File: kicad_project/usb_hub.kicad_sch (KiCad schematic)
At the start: 55 parts, among them J1 USB4105-GF-A, J2 UJ2-ADH-3-TH, U2 CY7C65632-48AXCT, U3 USBLC6-2SC6, U4 USBLC6-2SC6, U5 USBLC6-2SC6, U6 BD2221G-LBTR, U7 BD2221G-LBTR, X1 12.000MHz

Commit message: Kate's suggestions, part 1
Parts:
- removed C1, C2: 100nF, Capacitor_SMD:C_1206_3216Metric, symbol Device:C_Small
- removed C5, C8: 1u, Capacitor_SMD:C_1206_3216Metric, symbol Device:C_Small
- removed X1: 12.000MHz, Oscillator:Oscillator_SMD_Abracon_ASV-4Pin_7.0x5.1mm, symbol Oscillator:ASV-xxxMHz
- added C33, C34: 2.2uF, Capacitor_SMD:C_1206_3216Metric, symbol Device:C_Small
- added R48, R49: 1, Resistor_SMD:R_1206_3216Metric, symbol Device:R_US
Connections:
- net GND: now also R48.1, R49.1
- net HUB_VDD_A: now also C33.2, C34.2
- new net: C33.1, R48.2
- new net: C34.1, R49.2
- no-connect marks 9 -> 8
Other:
- note added: "Based on the reference design and review feedback, I assume that needed debouncing is: - 1x 10uF and 1x 1uF on VREG (which I assume is needed only if the internal regulator is used) - A 100nF for each VCC_A pin, plus 2x (2.2uF + 1 Ohm) on VCC_A, plus a ferrite bead - A 100nF for each VCC_D, plus a ferrite bead"
- note removed: "12MHz CMOS Oscillator"
- note removed: "The reference design seems to recommend: - 1x 10uF and 1x 1uF on VREG (which I assume is needed only if the internal regulator is used) - A 100nF for each VCC_A pin, plus 2x 1uF on VCC_A, plus a ferrite bead - A 100nF for each VCC_D, plus a ferrite bead"
- moved on the sheet: C3, C4, C6, C7, FB1, FB2

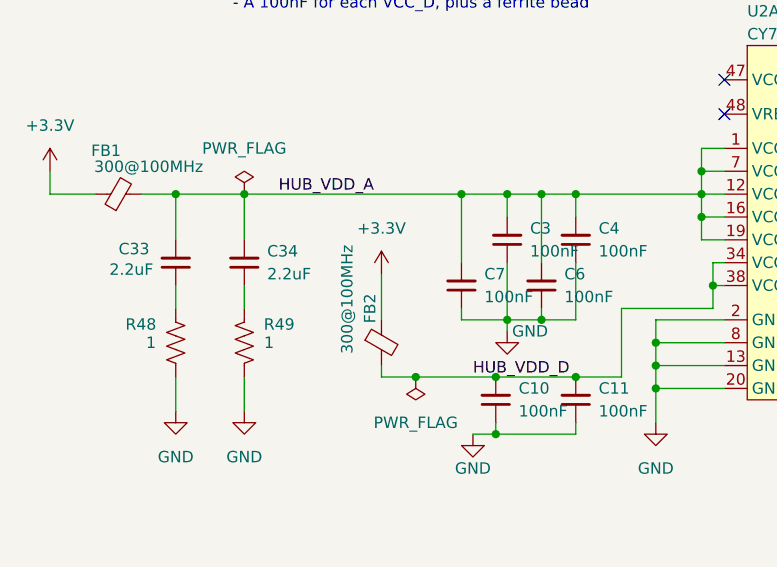
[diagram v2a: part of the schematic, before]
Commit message: Fix some unrouted nets
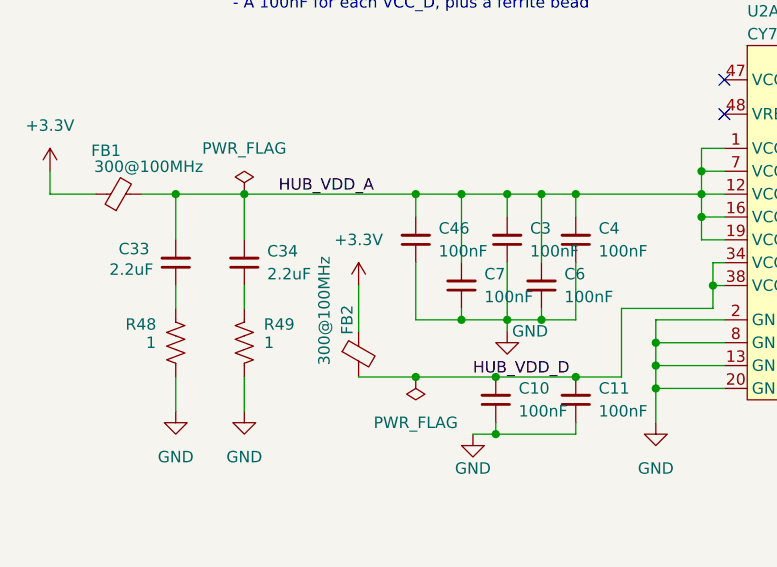
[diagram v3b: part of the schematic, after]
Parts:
- added C46: 100nF, Capacitor_SMD:C_1206_3216Metric, symbol Device:C_Small
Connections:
- net GND: now also C46.1
- net HUB_VDD_A: now also C46.2
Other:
- moved on the sheet: FB2
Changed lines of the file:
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@@
 	)
 	(junction
+		(at 58.42 48.26)
+		(diameter 0)
+		(color 0 0 0 0)
+	)
+	(junction
 		(at 72.39 48.26)
 		(diameter 0)
@@
 	)
 	(junction
+		(at 63.5 62.23)
+		(diameter 0)
+		(color 0 0 0 0)
+	)
+	(junction
 		(at 63.5 48.26)
 		(diameter 0)
@@
 	(wire
 		(pts
-			(xy 337.82 115.57) (xy 330.2 115.57)
+			(xy 58.42 62.23) (xy 58.42 55.88)
 		)
 		(stroke
@@
 	(wire
 		(pts
-			(xy 295.91 104.14) (xy 299.72 104.14)
+			(xy 337.82 115.57) (xy 330.2 115.57)
 		)
 		(stroke
@@
 	(wire
 		(pts
-			(xy 323.85 41.91) (xy 323.85 54.61)
+			(xy 295.91 104.14) (xy 299.72 104.14)
 		)
 		(stroke
@@
 	(wire
 		(pts
-			(xy 200.66 46.99) (xy 218.44 46.99)
+			(xy 323.85 41.91) (xy 323.85 54.61)
 		)
 		(stroke
@@
 	(wire
 		(pts
-			(xy 233.68 93.98) (xy 233.68 92.71)
+			(xy 200.66 46.99) (xy 218.44 46.99)
 		)
 		(stroke
@@
 	(wire
 		(pts
-			(xy 90.17 45.72) (xy 92.71 45.72)
+			(xy 233.68 93.98) (xy 233.68 92.71)
 		)
 		(stroke
@@
 	(wire
 		(pts
-			(xy 31.75 48.26) (xy 31.75 53.34)
+			(xy 90.17 45.72) (xy 92.71 45.72)
 		)
 		(stroke
@@
 	(wire
 		(pts
-			(xy 151.13 59.69) (xy 151.13 57.15)
+			(xy 31.75 48.26) (xy 31.75 53.34)
 		)
 		(stroke
@@
 	(wire
 		(pts
-			(xy 54.61 67.31) (xy 54.61 68.58)
+			(xy 151.13 59.69) (xy 151.13 57.15)
 		)
 		(stroke
@@
 	(wire
 		(pts
-			(xy 54.61 57.15) (xy 54.61 62.23)
+			(xy 52.07 58.42) (xy 52.07 63.5)
 		)
 		(stroke
@@
 	(wire
 		(pts
+			(xy 58.42 48.26) (xy 63.5 48.26)
+		)
+		(stroke
+			(width 0)
+			(type default)
+		)
+	)
+	(wire
+		(pts
 			(xy 355.6 49.53) (xy 360.68 49.53)
 		)
@@
 	(wire
 		(pts
-			(xy 54.61 68.58) (xy 58.42 68.58)
+			(xy 52.07 68.58) (xy 58.42 68.58)
 		)
 		(stroke
@@
 	(wire
 		(pts
-			(xy 39.37 48.26) (xy 63.5 48.26)
+			(xy 39.37 48.26) (xy 58.42 48.26)
 		)
 		(stroke
@@
 	(wire
 		(pts
+			(xy 58.42 48.26) (xy 58.42 50.8)
+		)
+		(stroke
+			(width 0)
+			(type default)
+		)
+	)
+	(wire
+		(pts
 			(xy 335.28 118.11) (xy 335.28 125.73)
 		)
@@
 	(wire
 		(pts
+			(xy 63.5 62.23) (xy 58.42 62.23)
+		)
+		(stroke
+			(width 0)
+			(type default)
+		)
+	)
+	(wire
+		(pts
 			(xy 85.09 64.77) (xy 92.71 64.77)
 		)
@@
 	)
 	(symbol
+		(lib_id "Device:C_Small")
+		(at 58.42 53.34 180)
+		(unit 1)
+		(exclude_from_sim no)
+		(in_bom yes)
+		(on_board yes)
+		(dnp no)
+		(fields_autoplaced yes)
+		(property "Reference" "C46"
+			(at 60.96 52.0636 0)
+			(effects
+				(font
+					(size 1.27 1.27)
+				)
+				(justify right)
+			)
+		)
+		(property "Value" "100nF"
+			(at 60.96 54.6036 0)
+			(effects
+				(font
+					(size 1.27 1.27)
+				)
+				(justify right)
+			)
+		)
+		(property "Footprint" "Capacitor_SMD:C_1206_3216Metric"
+			(at 58.42 53.34 0)
+			(effects
+				(font
+					(size 1.27 1.27)
+				)
+				(hide yes)
+			)
+		)
+		(property "Datasheet" "~"
+			(at 58.42 53.34 0)
+			(effects
+				(font
+					(size 1.27 1.27)
+				)
+				(hide yes)
+			)
+		)
+		(property "Description" "Unpolarized capacitor, small symbol"
+			(at 58.42 53.34 0)
+			(effects
+				(font
+					(size 1.27 1.27)
+				)
+				(hide yes)
+			)
+		)
+		(property "SKU" ""
+			(at 58.42 53.34 0)
+			(effects
+				(font
+					(size 1.27 1.27)
+				)
+				(hide yes)
+			)
+		)
+		(property "Supplier" "Digi-Key"
+			(at 58.42 53.34 0)
+			(effects
+				(font
+					(size 1.27 1.27)
+				)
+				(hide yes)
+			)
+		)
+		(property "LibRef" "GRM319R72A104KA01D"
+			(at 58.42 53.34 0)
+			(effects
+				(font
+					(size 1.27 1.27)
+				)
+				(hide yes)
+			)
+		)
+		(pin "1"
+		)
+		(pin "2"
+		)
+		(instances
+			(project "mbed-ce-ci-shield-v2"
+				(path "/a0f40274-9469-4bcf-885c-e8b8a490ea54/d2cb7c4f-a03f-4f1c-8cab-0427a0ad2909"
+					(reference "C46")
+					(unit 1)
+				)
+			)
+		)
+	)
+	(symbol
 		(lib_id "power:GND")
 		(at 156.21 105.41 0)
@@
 	(symbol
 		(lib_id "power:+3.3V")
-		(at 54.61 57.15 0)
+		(at 52.07 58.42 0)
 		(unit 1)
 		(exclude_from_sim no)
@@
 		(fields_autoplaced yes)
 		(property "Reference" "#PWR031"
-			(at 54.61 60.96 0)
+			(at 52.07 62.23 0)
 			(effects
 				(font
@@
 		)
 		(property "Value" "+3.3V"
-			(at 54.61 52.07 0)
+			(at 52.07 53.34 0)
 			(effects
 				(font
@@
 		)
 		(property "Footprint" ""
-			(at 54.61 57.15 0)
+			(at 52.07 58.42 0)
 			(effects
 				(font
@@
 		)
 		(property "Datasheet" ""
-			(at 54.61 57.15 0)
+			(at 52.07 58.42 0)
 			(effects
 				(font
@@
 		)
 		(property "Description" "Power symbol creates a global label with name \"+3.3V\""
-			(at 54.61 57.15 0)
+			(at 52.07 58.42 0)
 			(effects
 				(font
@@
 	(symbol
 		(lib_id "Device:FerriteBead_Small")
-		(at 54.61 64.77 0)
+		(at 52.07 66.04 0)
 		(unit 1)
 		(exclude_from_sim no)
@@
 		(dnp no)
 		(property "Reference" "FB2"
-			(at 53.34 60.96 90)
+			(at 50.8 62.23 90)
 			(effects
 				(font
@@
 		)
 		(property "Value" "300@100MHz"
-			(at 50.8 59.944 90)
+			(at 48.26 61.214 90)
 			(effects
 				(font
@@
 		)
 		(property "Footprint" "Resistor_SMD:R_1206_3216Metric"
-			(at 52.832 64.77 90)
+			(at 50.292 66.04 90)
 			(effects
 				(font
@@
 		)
 		(property "Datasheet" "~"
-			(at 54.61 64.77 0)
+			(at 52.07 66.04 0)
 			(effects
 				(font
@@
 		)
 		(property "Description" "Ferrite bead, small symbol"
-			(at 54.61 64.77 0)
+			(at 52.07 66.04 0)
 			(effects
 				(font
@@
 		)
 		(property "SKU" "732-4654-1-ND"
-			(at 54.61 64.77 0)
+			(at 52.07 66.04 0)
 			(effects
 				(font
@@
 		)
 		(property "Supplier" "Digi-Key"
-			(at 54.61 64.77 0)
+			(at 52.07 66.04 0)
 			(effects
 				(font
@@
 		)
 		(property "LibRef" "742792121"
-			(at 54.61 64.77 0)
+			(at 52.07 66.04 0)
 			(effects
 				(font

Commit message: Fix some BOM isues
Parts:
- R48, R49: LibRef P1.0RCT-ND -> ERJ-8RQF1R0V; SKU P120FCT-ND -> P1.0RCT-ND
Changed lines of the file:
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@@
 			)
 		)
-		(property "LibRef" "P1.0RCT-ND"
+		(property "LibRef" "ERJ-8RQF1R0V"
 			(at 31.75 64.77 0)
 			(effects
@@
 			)
 		)
-		(property "SKU" "P120FCT-ND"
+		(property "SKU" "P1.0RCT-ND"
 			(at 31.75 64.77 0)
 			(effects
@@
 			)
 		)
-		(property "LibRef" "P1.0RCT-ND"
+		(property "LibRef" "ERJ-8RQF1R0V"
 			(at 39.37 64.77 0)
 			(effects
@@
 			)
 		)
-		(property "SKU" "P120FCT-ND"
+		(property "SKU" "P1.0RCT-ND"
 			(at 39.37 64.77 0)
 			(effects

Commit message: Oops, fix wrong LibRef for 4.7k resistor
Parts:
- R14: LibRef ERJ-8ENF4702V -> ERJ-8ENF4701V
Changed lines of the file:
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@@
 			)
 		)
-		(property "LibRef" "ERJ-8ENF4702V"
+		(property "LibRef" "ERJ-8ENF4701V"
 			(at 24.13 121.92 0)
 			(effects
